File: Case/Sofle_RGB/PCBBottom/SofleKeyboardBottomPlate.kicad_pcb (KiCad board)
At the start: 2 copper layers, 143.4 x 111.8 mm, 15 parts

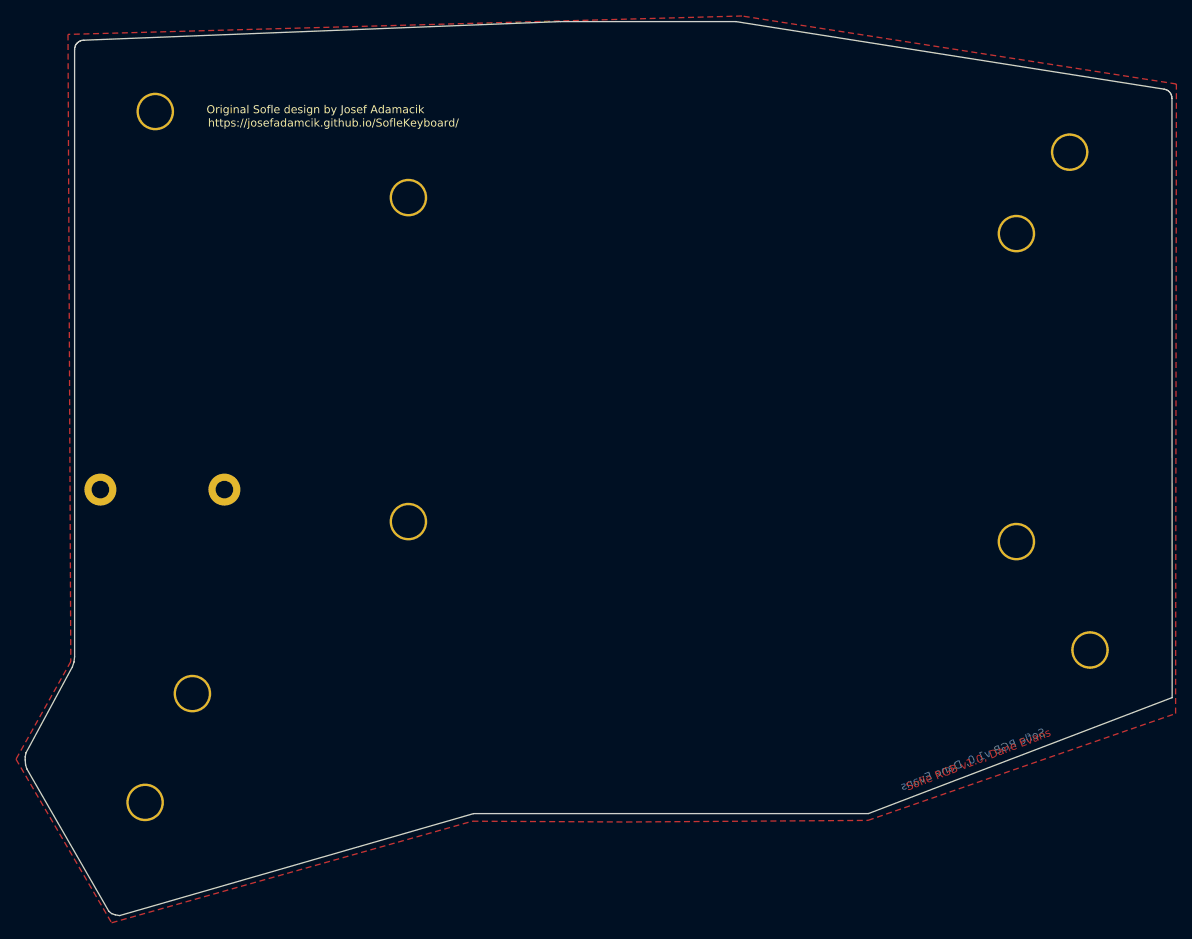
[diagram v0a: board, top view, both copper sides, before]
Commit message: fixed top and bottom plate hole sizes
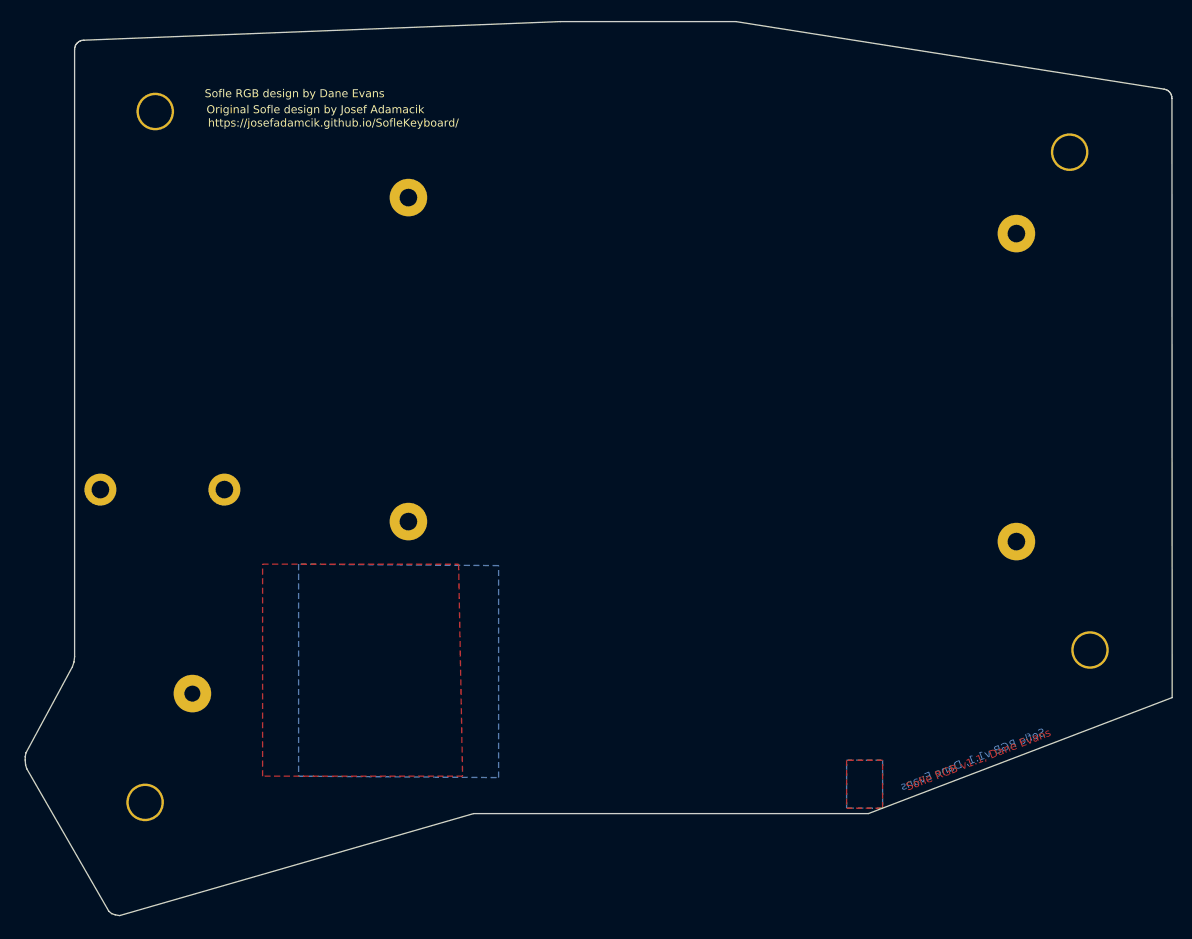
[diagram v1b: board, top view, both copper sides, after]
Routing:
- added copper zone on B.Cu, net (none)
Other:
- board text added: "Sofle RGB design by Dane Evans"
- board text added: "Sofle RGB v1.1, Dane Evans"
- board text removed: "Sofle RGB v1.0, Dane Evans"
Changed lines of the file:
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@@
   (general
     (thickness 1.6)
-    (drawings 41)
+    (drawings 45)
     (tracks 0)
     (zones 0)
@@
   (page A4)
   (layers
-    (0 F.Cu signal)
+    (0 F.Cu signal hide)
     (31 B.Cu signal)
     (32 B.Adhes user hide)
     (33 F.Adhes user hide)
     (34 B.Paste user)
-    (35 F.Paste user hide)
-    (36 B.SilkS user)
-    (37 F.SilkS user)
+    (35 F.Paste user)
+    (36 B.SilkS user hide)
+    (37 F.SilkS user hide)
     (38 B.Mask user)
-    (39 F.Mask user)
+    (39 F.Mask user hide)
     (40 Dwgs.User user hide)
     (41 Cmts.User user hide)
@@
     (mod_text_size 1 1)
     (mod_text_width 0.15)
-    (pad_size 4 4)
-    (pad_drill 2.2)
+    (pad_size 4.7 4.7)
+    (pad_drill 4.1)
     (pad_to_mask_clearance 0.2)
     (aux_axis_origin 0 0)
@@
       (effects (font (size 0.29972 0.29972) (thickness 0.0762)))
     )
-    (pad "" thru_hole circle (at -0.175 -0.025 90) (size 4.7 4.7) (drill 4.1) (layers *.Cu *.Mask Dwgs.User)
+    (pad "" thru_hole circle (at -0.175 -0.025 90) (size 4.7 4.7) (drill 2.2) (layers *.Cu *.Mask Dwgs.User)
       (clearance 0.3))
   )
@@
       (effects (font (size 0.29972 0.29972) (thickness 0.0762)))
     )
-    (pad "" thru_hole circle (at 0 0 180) (size 4.7 4.7) (drill 4.1) (layers *.Cu *.Mask Dwgs.User)
+    (pad "" thru_hole circle (at 0 0 180) (size 4.7 4.7) (drill 2) (layers *.Cu *.Mask Dwgs.User)
       (clearance 0.3))
   )
@@
       (effects (font (size 0.29972 0.29972) (thickness 0.0762)))
     )
-    (pad "" thru_hole circle (at -0.025 -0.075 90) (size 4.7 4.7) (drill 4.1) (layers *.Cu *.Mask Dwgs.User)
+    (pad "" thru_hole circle (at -0.025 -0.075 90) (size 4.7 4.7) (drill 2.2) (layers *.Cu *.Mask Dwgs.User)
       (clearance 0.3))
   )
@@
       (effects (font (size 0.29972 0.29972) (thickness 0.0762)))
     )
-    (pad "" thru_hole circle (at 0.025 -0.075 90) (size 4.7 4.7) (drill 4.1) (layers *.Cu *.Mask Dwgs.User)
+    (pad "" thru_hole circle (at 0.025 -0.075 90) (size 4.7 4.7) (drill 2.2) (layers *.Cu *.Mask Dwgs.User)
       (clearance 0.3))
   )
@@
       (effects (font (size 0.29972 0.29972) (thickness 0.0762)))
     )
-    (pad "" thru_hole circle (at -0.225 -0.275 90) (size 4.7 4.7) (drill 4.1) (layers *.Cu *.Mask Dwgs.User)
+    (pad "" thru_hole circle (at -0.225 -0.275 90) (size 4.7 4.7) (drill 2.2) (layers *.Cu *.Mask Dwgs.User)
       (clearance 0.3))
   )
-  (gr_text "Original Sofle design by Josef Adamacik" (at 119.105 48.585) (layer B.SilkS)
+  (gr_poly (pts (xy 143.5 132) (xy 111 133) (xy 111.5 102.5) (xy 143.5 102.5)) (layer Dwgs.User) (width 0.1))
+  (gr_poly (pts (xy 226.5 43) (xy 227.5 122) (xy 189 135.5) (xy 139.5 136) (xy 93.5 149) (xy 81 128) (xy 88 115) (xy 88 37.5) (xy 198 29.5)) (layer Dwgs.User) (width 0.1))
+  (gr_text "Sofle RGB design by Dane Evans" (at 127 44) (layer B.SilkS)
     (effects (font (size 1 1) (thickness 0.2)) (justify mirror))
   )
-  (gr_text https://josefadamcik.github.io/SofleKeyboard/ (at 121.355 46.915) (layer B.SilkS)
+  (gr_text "Sofle RGB design by Dane Evans" (at 116.5 44.665) (layer F.SilkS)
+    (effects (font (size 1 1) (thickness 0.2)))
+  )
+  (gr_text "Original Sofle design by Josef Adamacik" (at 124 45.5) (layer B.SilkS)
+    (effects (font (size 1 1) (thickness 0.2)) (justify mirror))
+  )
+  (gr_text https://josefadamcik.github.io/SofleKeyboard/ (at 121.355 47) (layer B.SilkS)
     (effects (font (size 1 1) (thickness 0.15)) (justify mirror))
   )
@@
     (effects (font (size 1 1) (thickness 0.2)))
   )
-  (gr_text "Sofle RGB v1.0, Dane Evans" (at 201.285 127.895 21) (layer B.Cu)
+  (gr_text "Sofle RGB v1.1, Dane Evans" (at 201.285 127.895 21) (layer B.Cu)
     (effects (font (size 1 1) (thickness 0.2)) (justify mirror))
   )
-  (gr_text "Sofle RGB v1.0, Dane Evans" (at 201.975 127.925 21) (layer F.Cu)
+  (gr_text "Sofle RGB v1.1, Dane Evans" (at 201.975 127.925 21) (layer F.Cu)
     (effects (font (size 1 1) (thickness 0.2)))
   )
@@
     (connect_pads (clearance 0.508))
     (min_thickness 0.254)
-    (fill yes (arc_segments 32) (thermal_gap 0.508) (thermal_bridge_width 0.508))
+    (fill yes (arc_segments 32) (thermal_gap 0.508) (thermal_bridge_width 0.508) (smoothing chamfer) (radius 4))
     (polygon
       (pts
-        (xy 81.675 127.875) (xy 93.625 148.325) (xy 138.725 135.625) (xy 157.975 135.725) (xy 188.175 135.525)
-        (xy 226.625 122.175) (xy 226.725 43.475) (xy 172.425 34.975) (xy 88.175 37.275) (xy 88.525 115.675)
+        (xy 137.5 130) (xy 112.5 130) (xy 112.5 103.5) (xy 137 103.5)
       )
     )
+  )
+  (zone (net 0) (net_name "") (layer B.Cu) (hatch edge 0.508)
+    (connect_pads (clearance 0.508))
+    (min_thickness 0.254)
+    (fill yes (arc_segments 32) (thermal_gap 0.508) (thermal_bridge_width 0.508) (smoothing chamfer) (radius 4))
+    (polygon
+      (pts
+        (xy 142 103.675) (xy 117 103.5) (xy 117 130) (xy 142 130.175)
+      )
+    )
+  )
+  (zone (net 0) (net_name "") (layer B.Cu) (hatch edge 0.508)
+    (connect_pads (clearance 0.508))
+    (min_thickness 0.254)
+    (fill yes (arc_segments 32) (thermal_gap 0.508) (thermal_bridge_width 0.508) (smoothing chamfer) (radius 4))
+    (polygon
+      (pts
+        (xy 190 134) (xy 185.5 134) (xy 185.5 128) (xy 190 128)
+      )
+    )
+  )
+  (zone (net 0) (net_name "") (layer F.Cu) (hatch edge 0.508)
+    (connect_pads (clearance 0.508))
+    (min_thickness 0.254)
+    (fill yes (arc_segments 32) (thermal_gap 0.508) (thermal_bridge_width 0.508) (smoothing chamfer) (radius 4))
+    (polygon
+      (pts
+        (xy 190 128) (xy 185.5 128) (xy 185.5 134) (xy 190 134)
+      )
+    )
